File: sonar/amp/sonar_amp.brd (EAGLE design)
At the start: 100 x 80 mm, 34 parts, among them IC1 ADR510ARTZ-REEL7, IC2 LMV797MMX/NOPB, IC3 S-817B20AY-B2-U, IC4 LMV797MMX/NOPB, X1 332-50, X2 332-50

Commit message: Routed most of the board. Missing connections to the Beaglebone
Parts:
- removed C3: 0.1u, SparkFun-Capacitors:CAP-PTH-SMALLEZ
- removed HYDRO1, HYDRO2: (no value), SONAR:2,54/1,0X2
- removed IC1: ADR510ARTZ-REEL7, SONAR:SOT23
- removed J1, J2: (no value), jumper:04C
- removed U$10, U$5: MCP4561, SONAR:MSOP8
- removed X1, X2: 332-50, con-garry:332-50
- added 1V: (no value), SONAR:LED_1206
- added C11: 470p, SparkFun-Capacitors:0805-CAP
- added C12: 1n, SparkFun-Capacitors:0805-CAP
- added C13: 10n, SparkFun-Capacitors:0805-CAP
- added IC5: LMV797, SONAR:TSSOP8
- added IC6: ADR510, SONAR:SOT23
- added R11: 20k, SparkFun-Resistors:0805
- added R12: 1k, SparkFun-Resistors:0805
- added R13: 4.7k, SparkFun-Resistors:0805
- added R14: 30, SparkFun-Resistors:0805
- added R2: 10k, SparkFun-Resistors:0805
- added U$11: 009276004021106CONN, SONAR:PUSHCONN4TERM
- added U$12: BEAGLE_BONE_BLACK_CAPE, SparkFun-Boards:BEAGLE_BONE_BLACK_CAPE
- added X3, X4: 332-50, con-garry:332-50
- C1: value 0.1u -> 1u; device SparkFun-Capacitors:CAP-PTH-SMALLEZ -> SparkFun-Capacitors:0805-CAP
- C10: value 5p -> 56p; device SparkFun-Capacitors:CAP-PTH-SMALLEZ -> SparkFun-Capacitors:0805-CAP
- C2: value 0.1u -> 5p; device SparkFun-Capacitors:CAP-PTH-SMALLEZ -> SparkFun-Capacitors:0805-CAP
- C4: value 1u -> 56p; device SparkFun-Capacitors:CAP-PTH-SMALLEZ -> SparkFun-Capacitors:0805-CAP
- C5: value 5p -> 470p; device SparkFun-Capacitors:CAP-PTH-SMALLEZ -> SparkFun-Capacitors:0805-CAP
- C6: value 56p -> 1n; device SparkFun-Capacitors:CAP-PTH-SMALLEZ -> SparkFun-Capacitors:0805-CAP
- C7: value 470p -> 10n; device SparkFun-Capacitors:CAP-PTH-SMALLEZ -> SparkFun-Capacitors:0805-CAP
- C8: value 1n -> 1u; device SparkFun-Capacitors:CAP-PTH-SMALLEZ -> SparkFun-Capacitors:0805-CAP
- C9: value 1n -> 5p; device SparkFun-Capacitors:CAP-PTH-SMALLEZ -> SparkFun-Capacitors:0805-CAP
- IC2, IC4: value LMV797MMX/NOPB -> LMV797
- IC3: value S-817B20AY-B2-U -> LMV797; device SONAR:TO92 -> SONAR:TSSOP8
- JP2, JP3: device jumper:JP1 -> pinhead:2X20
- R1: value 10k -> 1k; device SparkFun-Resistors:AXIAL-0.1 -> SparkFun-Resistors:0805
- R10, R5: value 10k -> 20k; device SparkFun-Resistors:AXIAL-0.1 -> SparkFun-Resistors:0805
- R3, R4, R9: device SparkFun-Resistors:AXIAL-0.1 -> SparkFun-Resistors:0805
- R6: value 20k -> 1k; device SparkFun-Resistors:AXIAL-0.1 -> SparkFun-Resistors:0805
- R7: value 1.2k -> 1k; device SparkFun-Resistors:AXIAL-0.1 -> SparkFun-Resistors:0805
- R8: value 1k -> 10k; device SparkFun-Resistors:AXIAL-0.1 -> SparkFun-Resistors:0805
- moved JP2 202.5 mm to (50.8, 65.4)
- moved JP3 162.2 mm to (50.8, 17.1)
- moved C10 152.5 mm to (55.9, 38.1), turned to 180 degrees
- moved R10 150.6 mm to (48.3, 38.1)
- moved R9 144.8 mm to (52.1, 38.1)
- moved JP1 141.9 mm to (35.8, 27.8), turned to 270 degrees
- moved R6 138.1 mm to (59.7, 30.5), turned to 180 degrees
- moved R8 136.4 mm to (44.5, 40.6)
- moved R7 129.6 mm to (40.6, 40.6)
- moved C9 124.4 mm to (44.5, 38.1)
- moved IC4 115.5 mm to (44.5, 45.7), turned to 270 degrees
- moved C8 113.5 mm to (36.8, 40.6)
- moved C4 94.0 mm to (55.9, 35.6), turned to 180 degrees
- moved R5 91.5 mm to (59.7, 35.6), turned to 180 degrees
- moved C7 90.4 mm to (59.7, 33.0), turned to 180 degrees
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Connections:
- removed net 2V: C1.1, IC2.4, IC3.3, IC4.4, J1.3, J2.3
- removed net 3.3V: C2.1, IC1.1, IC3.2, J1.1, J2.1, U$10.8, U$5.8, X1.3
- removed net OUT1: C5.2, IC2.1, R3.P$1, R4.P$2
- removed net OUT2: C7.2, C8.1, IC2.6, IC2.7
- removed net POA: J1.2, J2.2, U$10.5, U$5.5
- new net AMPOUT1: IC3.1, IC3.2, R6.1
- new net AMPOUT2: IC5.1, IC5.2, R12.1
- new net HYDRO1: C1.1, U$11.P$4, U$11.P$4@2
- new net HYDRO2: C8.1, U$11.P$1, U$11.P$1@2
- new net N$1: C11.2, R10.2, R9.1
- new net N$100: C5.1, C6.2, IC2.6, IC2.7
- new net N$101: C4.2, IC2.5, R3.2
- new net N$102: C2.2, IC2.1, R2.2, R4.1
- new net N$13: JP3.9
- new net N$14: JP3.11
- new net N$15: JP3.13
- new net N$16: JP3.15
- new net N$17: JP3.17
- new net N$18: JP3.19
- new net N$19: JP3.2
- new net N$20: JP3.4
- new net N$200: C11.1, C12.2, IC4.6, IC4.7
- new net N$201: C10.2, IC4.5, R9.2
- new net N$202: C9.2, IC4.1, R10.1, R8.2
- new net N$21: JP3.6
- new net N$22: JP3.8
- new net N$23: JP3.10
- new net N$24: JP3.12
- new net N$25: JP3.14
- new net N$26: JP3.16
- new net N$27: JP3.18
- new net N$28: JP3.20
- new net N$29: IC3.6
- new net N$3: C12.1, C13.2, R12.2
- new net N$30: IC3.5
- new net N$31: IC5.7
- new net N$32: IC5.6
- new net N$33: IC5.5
- new net N$34: 1V.C, R14.2
- new net N$9: U$12.P9.1
- new net POB1: C8.2, R7.1
- new net POW1: C9.1, IC4.2, R7.2, R8.1
- new net VCC: IC2.4, IC3.4, IC4.4, IC5.4, JP3.7, R13.2
- net 1V: now also 1V.A, IC4.3, IC6.1, R11.2, R13.1, R5.2; no longer C3.1, C6.2, IC1.2, IC4.5, R1.P$2, R6.P$1, R9.P$1
- net AGND: now also C10.1, C4.1, IC3.8, IC5.8, IC6.2, R14.1, U$11.P$2, U$11.P$2@2, U$11.P$3, U$11.P$3@2; no longer C1.2, C2.2, C3.2, HYDRO1.1, HYDRO2.2, IC1.3, IC3.1, JP2.1, JP3.1, U$10.4, U$5.4
- net GND: now also X3.1; no longer X1.1
- net GPIO_48: now also X3.15; no longer X1.15
- net GPIO_49: now also X3.23; no longer U$10.1, U$5.1, X1.23
- net I2C2_SCL: now also X3.19; no longer U$10.2, U$5.2, X1.19
- net I2C_SDA: now also X3.20; no longer U$10.3, U$5.3, X1.20
- net N$10: now also JP3.3; no longer R8.P$1, R9.P$2
- net N$11: now also JP3.5; no longer C10.1, IC4.6, R10.P$2, R8.P$2
- net N$12: now also IC3.7; no longer C10.2, HYDRO2.1, IC4.7, R10.P$1
- net N$2: now also C5.2, R3.1, R4.2; no longer C7.1, R4.P$1, R5.P$2
- net N$4: now also IC6.3; no longer C6.1, IC2.5, R5.P$1
- net N$5: now also C13.1, IC5.3, R11.1; no longer C4.1, HYDRO1.2
- net N$6: now also C6.1, C7.2, R6.2; no longer C8.2, C9.1, R7.P$2
- net N$7: now also C7.1, IC3.3, R5.1; no longer C9.2, IC4.3, R6.P$2
- net N$8: now also JP3.1; no longer IC4.1, IC4.2, R7.P$1
- net POB: now also C1.2, R1.1; no longer C4.2, JP2.2, JP3.2, R1.P$1, U$10.7, U$5.7
- net POW: now also C2.1, R1.2, R2.1; no longer C5.1, R3.P$2, U$10.6, U$5.6
- net PWR_BUT: now also X3.9; no longer X1.9
- net SYS5V: now also X3.7; no longer X1.7
- net VDD5V: now also X3.5; no longer X1.5
- net VDD_ADC: now also X3.32; no longer X1.32
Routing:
- net 1V: track 0.00 -> 80.2 mm
- net N$202: track 0.00 -> 26.7 mm, vias 0 -> 2
- net AGND: track 0.00 -> 23.3 mm, vias 0 -> 9
- net POW1: track 0.00 -> 16.1 mm, vias 0 -> 2
- net N$101: track 0.00 -> 16.1 mm, vias 0 -> 2
- net POW: track 0.00 -> 13.4 mm
- net N$100: track 0.00 -> 12.2 mm
- net N$201: track 0.00 -> 12.1 mm
- net N$102: track 0.00 -> 11.5 mm
- net N$200: track 0.00 -> 11.2 mm
- net N$7: track 0.00 -> 10.1 mm
- net N$5: track 0.00 -> 9.91 mm
- net AMPOUT1: track 0.00 -> 7.26 mm
- net N$2: track 0.00 -> 4.55 mm
- net N$1: track 0.00 -> 4.55 mm
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- added copper zone on layer 16, net AGND
- added copper zone on layer 1, net VCC
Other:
- board size 100 x 80 mm -> 101.3 x 81.3 mm

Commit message: Non-BNC amp board. Laid over PRUDAQ layout for reference. Need to add PWM header for servo next.
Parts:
- removed JP1: (no value), jumper:JP1
- removed JP2, JP3: (no value), pinhead:2X20
- removed X3, X4: 332-50, con-garry:332-50
- added 1V-TIE: 0R-JUMPC, jump-0r-smd:C0R-JMP
- added GNDTIE: (no value), eagle-ltspice:R0402
- added LEFT: (no value), pinhead:2X20
- added MID: (no value), pinhead:2X05
- added ZD1, ZD2: CDZV2.0B, SONAR:SOD-923
- moved U$12 1.27 mm to (7.62, 14.0)
- moved U$11 0.64 mm to (26.0, 41.9)
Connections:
- removed net GND: JP1.2, X3.1
- removed net GPIO_48: X3.15
- removed net GPIO_49: X3.23
- removed net I2C2_SCL: X3.19
- removed net I2C_SDA: X3.20
- removed net N$9: U$12.P9.1
- removed net PWR_BUT: X3.9
- removed net SYS5V: X3.7
- removed net VDD5V: X3.5
- removed net VDD_ADC: X3.32
- new net DGND: GNDTIE.2, U$12.P9.1
- new net IN0: MID.2
- new net IN1: MID.4
- new net IN2: MID.6
- new net IN3: MID.8
- new net IN4: MID.10
- new net INDEP_1V: 1V-TIE.3, IC6.1, R13.1
- new net VREF: 1V-TIE.1, MID.9
- net 1V: now also 1V-TIE.2; no longer IC6.1, R13.1
- net AGND: now also GNDTIE.1, MID.1, ZD1.A, ZD2.A; no longer JP1.1
- net AMPOUT1: now also ZD1.C
- net AMPOUT2: now also ZD2.C
- net N$10: now also LEFT.3; no longer JP3.3
- net N$11: now also LEFT.5; no longer JP3.5
- net N$13: now also LEFT.9; no longer JP3.9
- net N$14: now also LEFT.11; no longer JP3.11
- net N$15: now also LEFT.13; no longer JP3.13
- net N$16: now also LEFT.15; no longer JP3.15
- net N$17: now also LEFT.17; no longer JP3.17
- net N$18: now also LEFT.19; no longer JP3.19
- net N$19: now also LEFT.2; no longer JP3.2
- net N$20: now also LEFT.4; no longer JP3.4
- net N$21: now also LEFT.6; no longer JP3.6
- net N$22: now also LEFT.8; no longer JP3.8
- net N$23: now also LEFT.10; no longer JP3.10
- net N$24: now also LEFT.12; no longer JP3.12
- net N$25: now also LEFT.14; no longer JP3.14
- net N$26: now also LEFT.16; no longer JP3.16
- net N$27: now also LEFT.18; no longer JP3.18
- net N$28: now also LEFT.20; no longer JP3.20
- net N$8: now also LEFT.1; no longer JP3.1
- net VCC: now also LEFT.7; no longer JP3.7
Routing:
- net DGND: track 0.00 -> 46.3 mm, vias 0 -> 1
- net VREF: track 0.00 -> 34.0 mm
- net INDEP_1V: track 0.00 -> 17.2 mm
- net AGND: track 23.3 -> 32.7 mm, vias 9 -> 10
- net AMPOUT2: track 4.12 -> 12.5 mm, vias 0 -> 2
- net AMPOUT1: track 7.26 -> 15.3 mm
- net 1V: track 80.2 -> 88.1 mm, vias 0 -> 2
- net HYDRO2: track 2.25 -> 1.61 mm
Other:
- outline, holes or cut-outs redrawn
- board text added: "IN0"
- board text added: "IN4"
- board text added: "REG"
- board text added: "VREF"

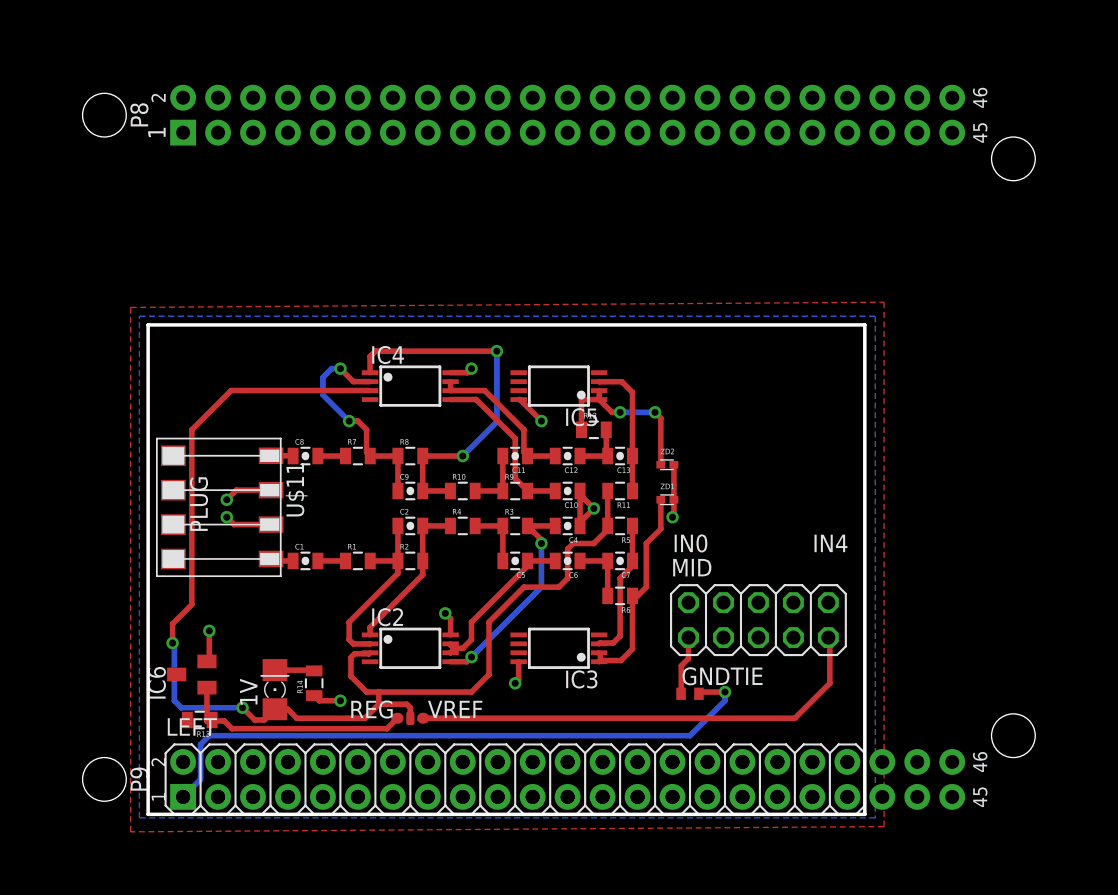
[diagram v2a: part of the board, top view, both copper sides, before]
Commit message: Added PWM, silkscreen to board. Input connection is flying lead, next iteration will have BNC inputs
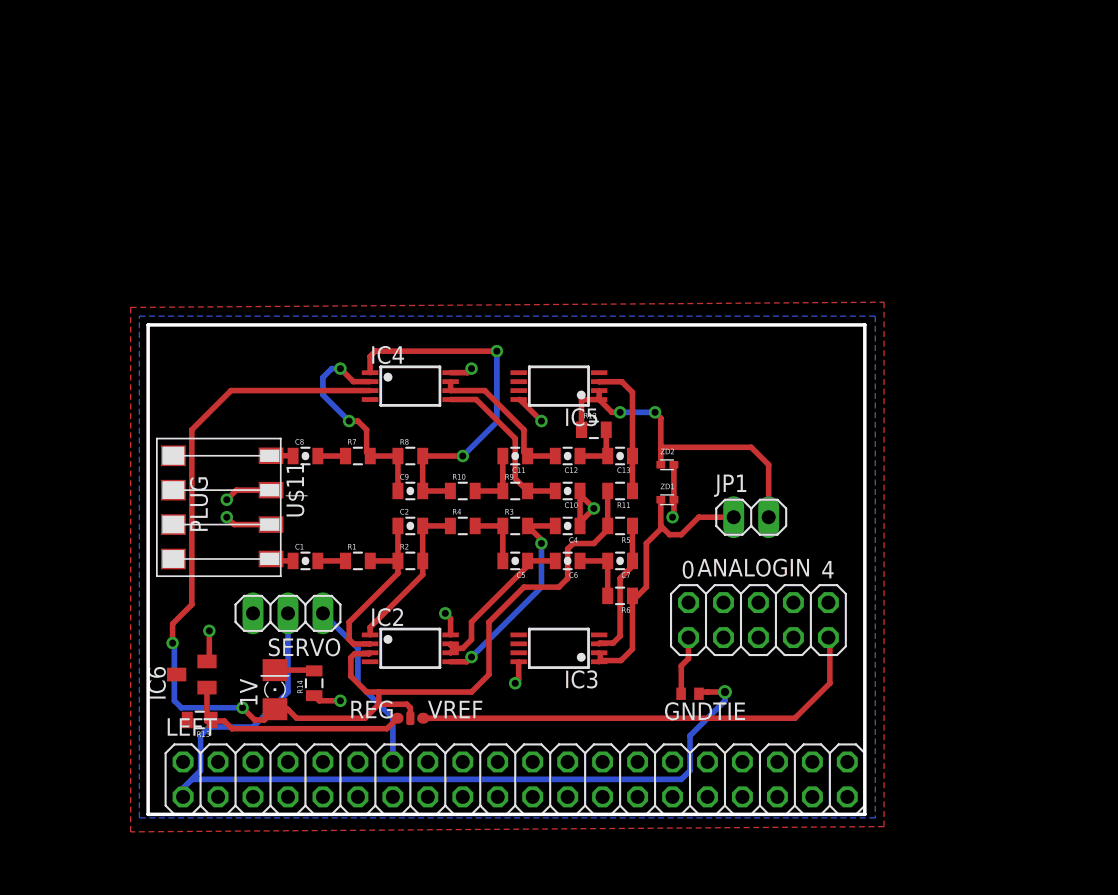
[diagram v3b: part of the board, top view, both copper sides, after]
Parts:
- removed U$12: BEAGLE_BONE_BLACK_CAPE, SparkFun-Boards:BEAGLE_BONE_BLACK_CAPE
- added JP1: (no value), pinhead:1X02
- added SERVO: (no value), pinhead:1X03
- renumbered MID to ANALOGIN
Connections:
- net N$10 renamed VDD_3V3
- net N$13 renamed PWR_BUT
- net N$14 renamed GPIO_30
- net N$15 renamed GPIO_31
- net N$16 renamed GPIO_48
- net N$17 renamed GPIO4
- net N$18 renamed I2C2_SCL
- net N$23 renamed SYS_!RESETN
- net N$24 renamed GPIO_60
- net N$26 renamed EHRPWM1B
- net N$27 renamed GPIO_5
- net N$28 renamed I2C2_SDA
- removed net N$11: LEFT.5
- removed net N$25: LEFT.14
- removed net N$8: LEFT.1
- new net AIN0: LEFT.39
- new net AIN1: LEFT.40
- new net AIN2: LEFT.37
- new net AIN3: LEFT.38
- new net AIN4: LEFT.33
- new net AIN5: LEFT.36
- new net AIN6: LEFT.35
- new net EHRPWM1A: LEFT.14, SERVO.1
- new net GNDA_ADC: LEFT.34
- new net GPIO_117: LEFT.25
- new net GPIO_120: LEFT.31
- new net GPIO_121: LEFT.29
- new net GPIO_122: LEFT.30
- new net GPIO_123: LEFT.28
- new net GPIO_125: LEFT.27
- new net GPIO_14: LEFT.26
- new net GPIO_15: LEFT.24
- new net GPIO_2: LEFT.22
- new net GPIO_3: LEFT.21
- new net GPIO_49: LEFT.23
- new net SYS_5V: LEFT.7
- new net VDD_ADC: LEFT.32
- net AMPOUT1: now also JP1.1
- net AMPOUT2: now also JP1.2
- net DGND: now also LEFT.1, SERVO.2; no longer U$12.P9.1
- net VCC: now also LEFT.5, SERVO.3; no longer LEFT.7
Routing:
- net DGND: track 46.3 -> 63.5 mm
- net EHRPWM1A: track 0.00 -> 12.9 mm
- net AMPOUT2: track 12.5 -> 24.7 mm
- net AMPOUT1: track 15.3 -> 21.4 mm
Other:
- board text added: "0"
- board text added: "4"
- board text added: "ARVP SONAR 2017 Amp/Filter Mike Bardwell"
- board text added: "| AGND |"
- board text added: "|1V|"
- board text removed: "IN0"
- board text removed: "IN4"

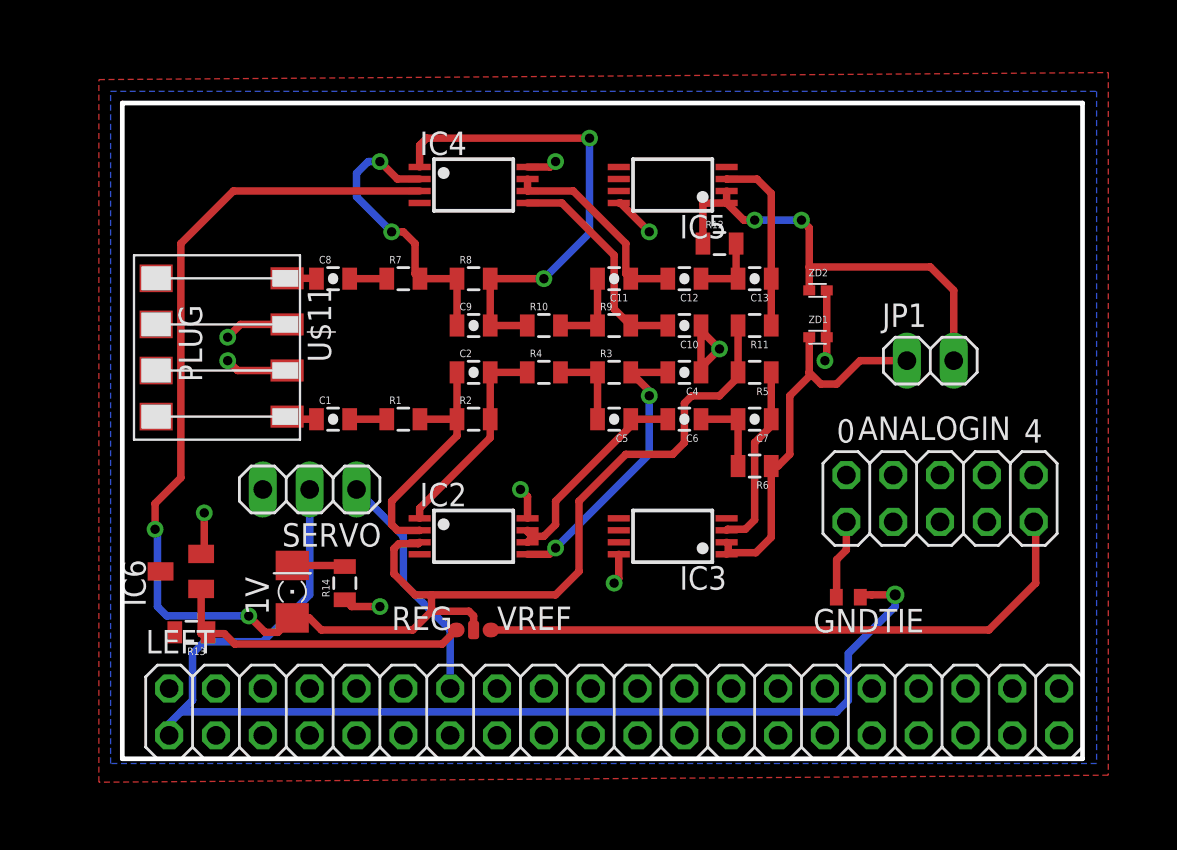
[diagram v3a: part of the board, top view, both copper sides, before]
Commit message: Replaced flying lead with BNC conn. Passes APC DRU (7 mil minimums, standard drill sizes on site). Removed 1V LED (no 1V LED's on digikey)
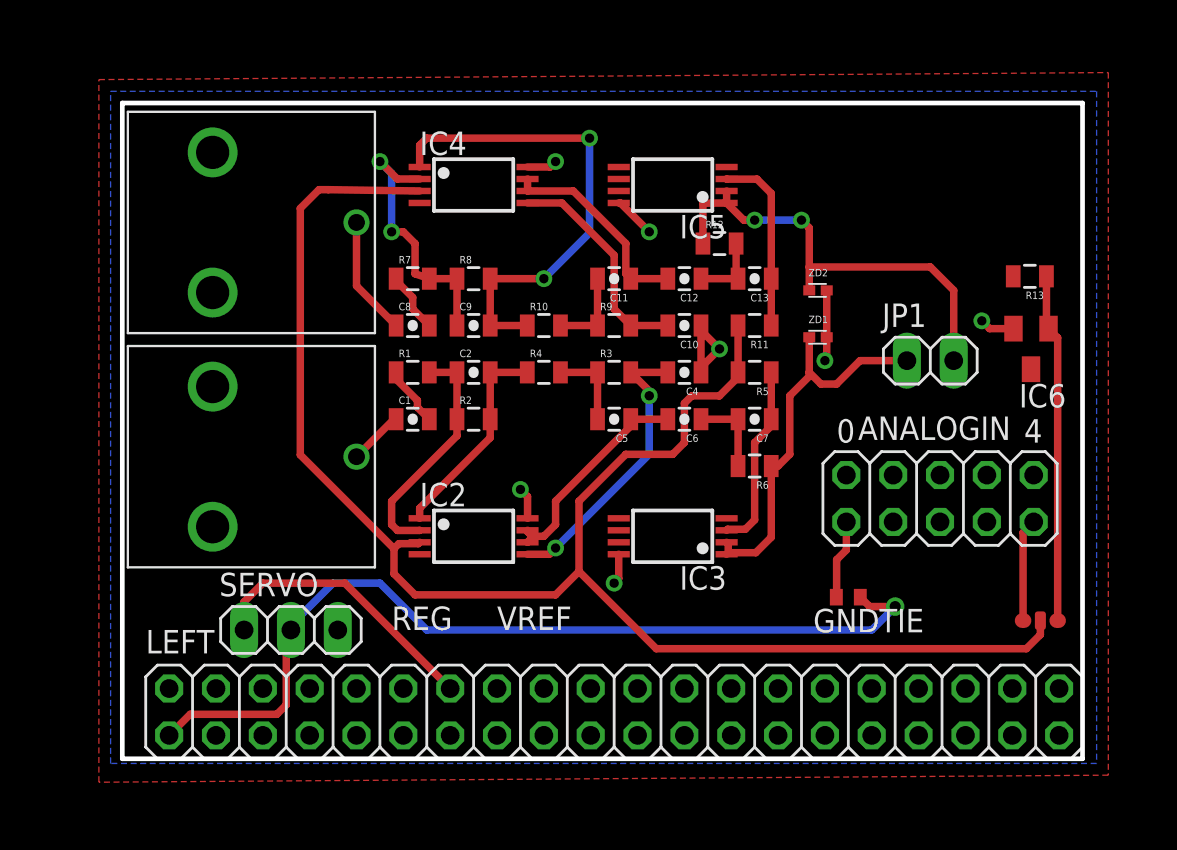
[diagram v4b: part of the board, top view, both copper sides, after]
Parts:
- removed 1V: (no value), SONAR:LED_1206
- removed R14: 30, SparkFun-Resistors:0805
- removed U$11: 009276004021106CONN, SONAR:PUSHCONN4TERM
- added U$12, U$8: MOLEX-0731000105, SONAR:BNC-CONN
- moved R13 49.4 mm to (74.6, 40.8)
- moved IC6 47.7 mm to (74.7, 36.8), turned to 180 degrees
- moved 1V-TIE 30.7 mm to (75.2, 22.1), turned to 90 degrees
- moved SERVO 7.69 mm to (34.5, 21.6), turned to 0 degrees
- moved C8 5.01 mm to (41.1, 38.1)
- moved C1 4.32 mm to (41.1, 33.0)
- moved R1 2.59 mm to (41.1, 35.6)
- moved R7 0.51 mm to (41.1, 40.6)
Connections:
- removed net N$34: 1V.C, R14.2
- net 1V: no longer 1V.A
- net AGND: now also U$12.P$2, U$12.P$3, U$8.P$2, U$8.P$3; no longer R14.1, U$11.P$2, U$11.P$2@2, U$11.P$3, U$11.P$3@2
- net HYDRO1: now also U$8.P$1; no longer U$11.P$4, U$11.P$4@2
- net HYDRO2: now also U$12.P$1; no longer U$11.P$1, U$11.P$1@2
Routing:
- net VREF: track 34.0 -> 5.74 mm
- net DGND: track 63.5 -> 48.8 mm
- net AGND: track 32.7 -> 23.3 mm, vias 10 -> 7
- net HYDRO2: track 1.61 -> 6.48 mm
- net N$34: track 2.87 -> 0.00 mm
- net EHRPWM1A: track 12.9 -> 15.5 mm
- net INDEP_1V: track 17.2 -> 18.9 mm
- net POW1: track 16.1 -> 14.7 mm
- net POB: track 2.01 -> 3.29 mm
- net POB1: track 2.01 -> 3.29 mm
- net POW: track 13.4 -> 12.9 mm
- net 1V: track 88.1 -> 88.5 mm, vias 2 -> 0
